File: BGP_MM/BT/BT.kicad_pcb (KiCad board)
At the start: 2 copper layers, 26 x 26 mm, 36 parts, among them J1 Conn_01x02_Male, J2 Conn_01x02_Male, J3 Conn_01x04_Male, J4 Conn_01x04_Male, Q1 MMBF5457, U1 MC33178

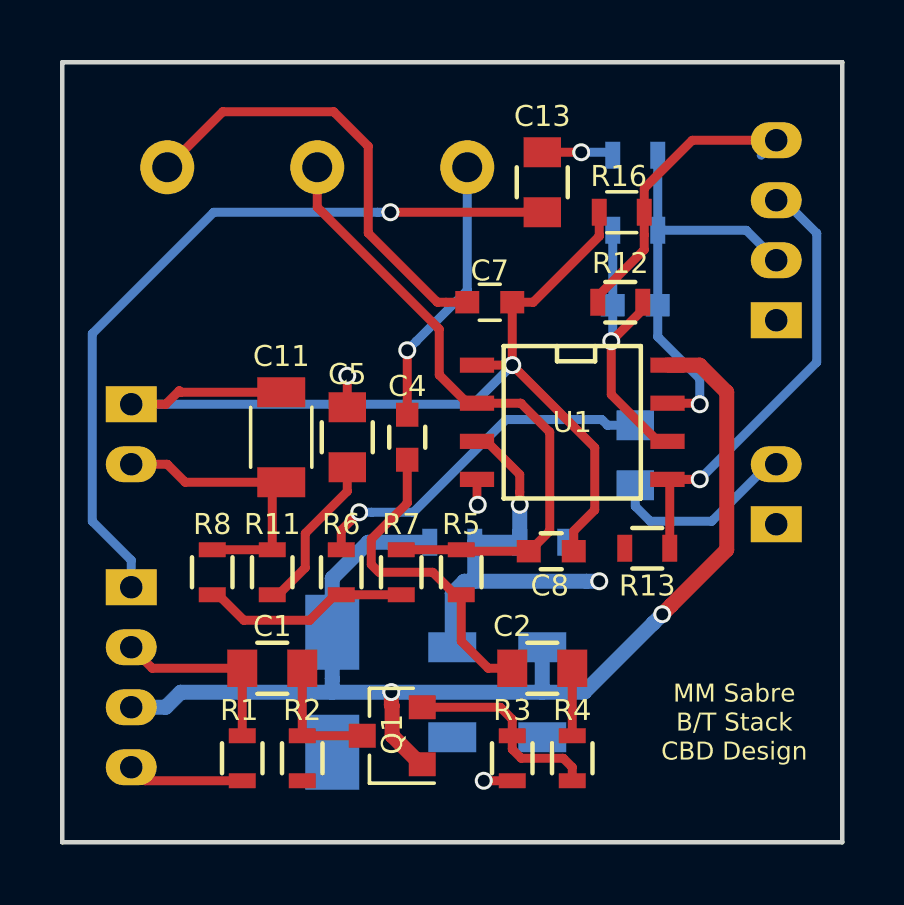
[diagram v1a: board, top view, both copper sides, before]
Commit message: BT Bright Cap/Res changed
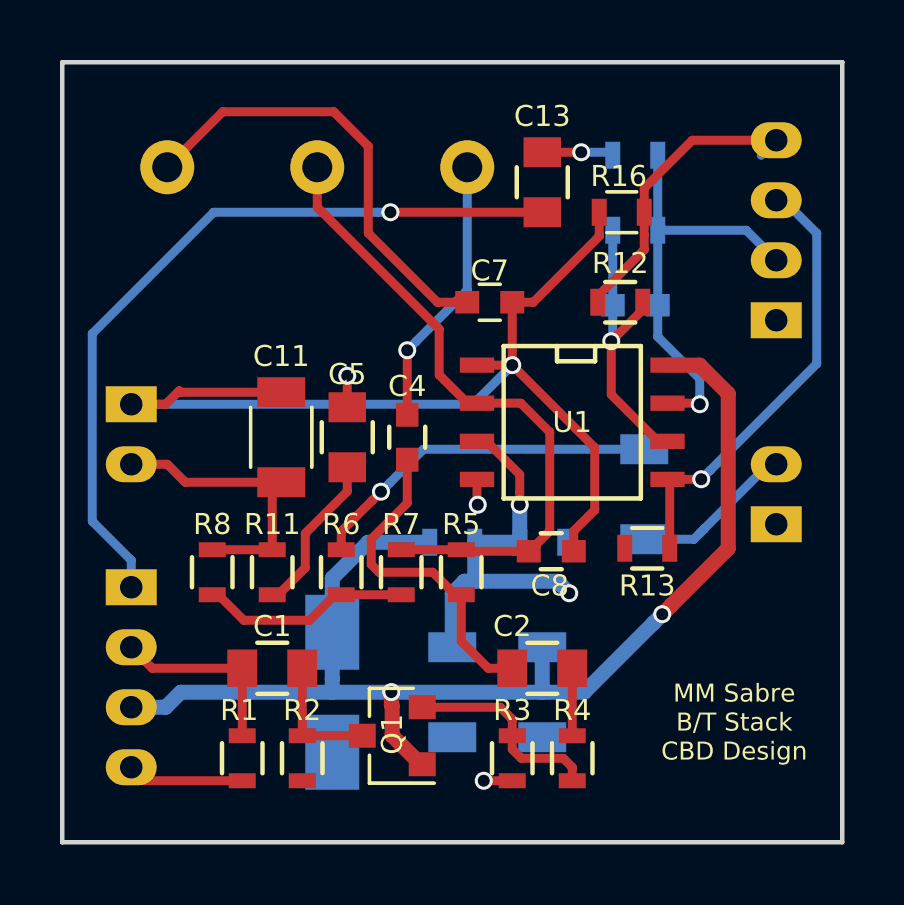
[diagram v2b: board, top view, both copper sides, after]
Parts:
- C3: value 10n -> 22n; footprint Capacitors_SMD:C_0805 -> Capacitors_SMD:C_1206
- R12, R14: value 22k -> 20k
- R6: value 2k -> 1k
- moved C3 1.33 mm to (164.4, 100.4)
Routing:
- net /Vref: track 13.8 -> 13.0 mm
- net Net-(C3-Pad2): track 6.39 -> 5.65 mm

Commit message: MM Refactoring
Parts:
- removed C12: 120p, Capacitors_SMD:C_0603
- removed C13: 1u, Capacitors_SMD:C_0805
- removed J4: Conn_01x04_Male, Connectors_JST:JST_PH_B4B-PH-K_04x2.00mm_Straight
- removed Q1: MMBF5457, TO_SOT_Packages_SMD:SOT-23
- removed R11: 10k, Resistors_SMD:R_0603
- removed R12, R14: 20k, Resistors_SMD:R_0603
- removed R13: 200k, Resistors_SMD:R_0603
- removed R15: 1k, Resistors_SMD:R_0603
- removed R16: 100, Resistors_SMD:R_0603
- added C10: 47n, Capacitors_SMD:C_1206, F.Cu at (165.0, 94.0)
- C1: value 0.1u -> 1u
- C11: value 47n -> 10u; footprint Capacitors_SMD:C_1206 -> Capacitors_SMD:C_0805
- C2: value 1u -> 120p; footprint Capacitors_SMD:C_0805 -> Capacitors_SMD:C_0603_HandSoldering
- C3: moved to F.Cu
- C4: footprint Capacitors_SMD:C_0603 -> Capacitors_SMD:C_0805
- C6, C9: value 47u -> 10u; footprint Capacitors_SMD:C_1206 -> Capacitors_SMD:C_0805
- C7, C8: footprint Capacitors_SMD:C_0603 -> Capacitors_SMD:C_0603_HandSoldering
- J2: value Conn_01x02_Male -> Conn_01x04_Male; footprint Connectors_JST:JST_PH_B2B-PH-K_02x2.00mm_Straight -> Connectors_JST:JST_PH_B4B-PH-K_04x2.00mm_Straight
- J3: value Conn_01x04_Male -> Conn_01x02_Male; footprint Connectors_JST:JST_PH_B4B-PH-K_04x2.00mm_Straight -> Connectors_JST:JST_PH_B2B-PH-K_02x2.00mm_Straight
- R1: footprint Resistors_SMD:R_0603 -> Capacitors_SMD:C_0603_HandSoldering
- R10: value 20k -> 1k; footprint Resistors_SMD:R_0603 -> Capacitors_SMD:C_0603_HandSoldering; moved to F.Cu
- R2: value 1MEG -> 470k; footprint Resistors_SMD:R_0603 -> Capacitors_SMD:C_0603_HandSoldering
- R3: value 20k -> 220k; footprint Resistors_SMD:R_0603 -> Capacitors_SMD:C_0603_HandSoldering
- R4: value 100 -> 1k; footprint Resistors_SMD:R_0603 -> Capacitors_SMD:C_0603_HandSoldering
- R5: value 220k -> 100k; footprint Resistors_SMD:R_0603 -> Capacitors_SMD:C_0603_HandSoldering
- R6: value 1k -> 2k; footprint Resistors_SMD:R_0603 -> Capacitors_SMD:C_0603_HandSoldering
- R7: footprint Resistors_SMD:R_0603 -> Capacitors_SMD:C_0603_HandSoldering; moved to B.Cu
- R8: value 2k -> 100k; footprint Resistors_SMD:R_0603 -> Capacitors_SMD:C_0603_HandSoldering; moved to B.Cu
- R9: value 20k -> 10k; footprint Resistors_SMD:R_0603 -> Capacitors_SMD:C_0603_HandSoldering; moved to F.Cu
- moved R3 13.8 mm to (152.0, 98.0), turned to 90 degrees
- moved C5 12.7 mm to (166.0, 104.0), turned to 270 degrees
- moved R8 11.5 mm to (159.8, 109.0), turned to 180 degrees
- moved J1 11.2 mm to (165.7, 90.6)
- moved C7 11.0 mm to (163.9, 104.0), turned to 90 degrees
- moved R6 10.9 mm to (164.0, 98.0), turned to 270 degrees
- moved C3 9.15 mm to (161.0, 108.9), turned to 90 degrees
- moved R9 9.03 mm to (166.1, 98.0), turned to 270 degrees
- moved U1 8.90 mm to (155.0, 103.5)
- moved C6 8.83 mm to (152.3, 105.5), turned to 0 degrees
- moved C9 7.16 mm to (165.0, 105.5), turned to 0 degrees
- moved R5 5.68 mm to (161.0, 98.0)
- moved R10 5.00 mm to (158.0, 98.0), turned to 90 degrees
- moved J3 4.40 mm to (147.2, 107.9)
- moved R7 4.30 mm to (159.8, 105.5), turned to 0 degrees
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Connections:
- C3 pad 2: Net-(C3-Pad2) -> /BR_O
- C4 pad 1: Net-(C2-Pad2) -> Net-(C2-Pad1)
- C7 pad 2: Net-(C11-Pad2) -> Net-(C10-Pad2)
- C8 pad 2: Net-(C11-Pad2) -> Net-(C10-Pad2)
- J1 pad 1: Earth -> Net-(C10-Pad2)
- J1 pad 2: Net-(C3-Pad2) -> Net-(C10-Pad1)
- J2 pad 1: Net-(C11-Pad2) -> /BR_O
- J2 pad 2: Net-(C11-Pad1) -> /SIG_I
- J3 pad 1: Net-(C13-Pad2) -> Earth
- J3 pad 2: /SIG_I -> VCC
- R1 pad 1: /SIG_I -> Net-(C2-Pad2)
- R1 pad 2: Earth -> Net-(C1-Pad1)
- R10 pad 1: /Vref -> Net-(C11-Pad1)
- R10 pad 2: Earth -> Net-(C10-Pad2)
- R2 pad 1: Net-(C1-Pad1) -> Net-(C2-Pad1)
- R2 pad 2: /Vref -> Net-(C2-Pad2)
- R3 pad 1: Net-(Q1-Pad2) -> Net-(C8-Pad1)
- R3 pad 2: Earth -> Net-(C2-Pad1)
- R4 pad 1: Net-(C2-Pad1) -> Net-(R4-Pad1)
- R4 pad 2: Net-(Q1-Pad2) -> Net-(C3-Pad1)
- R5 pad 1: Net-(C8-Pad1) -> Net-(R4-Pad1)
- R5 pad 2: Net-(C2-Pad2) -> Net-(C8-Pad1)
- R6 pad 1: Net-(R6-Pad1) -> Net-(C10-Pad1)
- R6 pad 2: Net-(C3-Pad1) -> Net-(R4-Pad1)
- R7 pad 1: Net-(R6-Pad1) -> VCC
- R7 pad 2: Net-(C8-Pad1) -> /Vref
- R8 pad 1: Net-(C11-Pad1) -> /Vref
- R8 pad 2: Net-(R6-Pad1) -> Earth
- R9 pad 1: VCC -> Net-(C10-Pad1)
- R9 pad 2: /Vref -> Net-(C5-Pad1)
- U1 pad 1: Net-(C11-Pad2) -> Net-(C2-Pad1)
- U1 pad 2: Net-(C8-Pad1) -> Net-(C2-Pad2)
- U1 pad 5: /Mr -> /Vref
- U1 pad 6: Net-(C12-Pad2) -> Net-(C8-Pad1)
- U1 pad 7: /Mo -> Net-(C10-Pad2)
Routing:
- net /BR_O: track 0.00 -> 32.6 mm, vias 0 -> 1
- net Net-(C10-Pad2): track 0.00 -> 26.7 mm
- net Net-(C13-Pad2): track 25.7 -> 0.00 mm, vias 1 -> 0
- net Net-(C11-Pad2): track 34.5 -> 13.6 mm, vias 1 -> 0
- net Net-(C7-Pad1): track 15.1 -> 31.6 mm, vias 0 -> 1
- net VCC: track 41.6 -> 25.7 mm, vias 2 -> 1
- net Net-(C2-Pad1): track 2.25 -> 17.4 mm
- net /Mr: track 15.1 -> 0.00 mm, vias 1 -> 0
- net /Mo: track 14.3 -> 0.00 mm, vias 1 -> 0
- net Net-(R4-Pad1): track 0.00 -> 14.1 mm
- net /SIG_I: track 6.24 -> 19.3 mm
- net Net-(C10-Pad1): track 0.00 -> 11.7 mm
- net /Mi: track 10.5 -> 0.00 mm
- net Net-(C12-Pad2): track 9.75 -> 0.00 mm, vias 1 -> 0
- net Net-(C8-Pad1): track 21.6 -> 31.3 mm, vias 0 -> 3
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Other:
- board size 26 x 26 mm -> 23 x 26 mm
- board text removed: "MM Sabre B/T Stack CBD Design"

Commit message: MM Refactoring
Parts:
- removed J3: Conn_01x02_Male, Connectors_JST:JST_PH_B2B-PH-K_02x2.00mm_Straight
- C1: value 1u -> 0.1u
- C2: value 120p -> 10p
- C3: value 22n -> 2.7n; footprint Capacitors_SMD:C_1206 -> Capacitors_SMD:C_0805
- C6, C9: footprint Capacitors_SMD:C_0805 -> Capacitors_SMD:C_1206
- J1: footprint Connectors_JST:JST_PH_B2B-PH-K_02x2.00mm_Straight -> Pin_Headers:Pin_Header_Straight_2x01_Pitch2.54mm
- J2: value Conn_01x04_Male -> Conn_01x05_Male; footprint Connectors_JST:JST_PH_B4B-PH-K_04x2.00mm_Straight -> Pin_Headers:Pin_Header_Straight_1x05_Pitch2.54mm
- R10: value 1k -> 100
- R4: value 1k -> 4.7k
- R6: value 2k -> 10k
- U1: value MC33178 -> TS512A
- moved J2 11.0 mm to (148.0, 108.5), turned to 0 degrees
- moved C10 4.34 mm to (161.6, 91.3), turned to 90 degrees
- moved C9 3.50 mm to (165.0, 109.0)
- moved C6 1.02 mm to (153.3, 105.7)
- moved J1 0.92 mm to (165.0, 90.0), turned to 270 degrees
- moved R7 0.51 mm to (159.9, 106.0)
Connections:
- J2 pad 1: /BR_O -> VCC
- J2 pad 2: /SIG_I -> /BR_O
- J2 pad 3: Net-(C11-Pad2) -> /SIG_I
- J2 pad 4: Earth -> Net-(C11-Pad2)
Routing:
- net /BR_O: track 32.6 -> 19.0 mm, vias 1 -> 0
- net /SIG_I: track 19.3 -> 8.33 mm
- net Earth: track 4.61 -> 2.18 mm
- net Net-(C10-Pad1): track 11.7 -> 10.7 mm
- net Net-(C2-Pad1): track 17.4 -> 18.1 mm
- net VCC: track 25.7 -> 25.0 mm
- net Net-(C11-Pad2): track 13.6 -> 13.0 mm
- net Net-(R4-Pad1): track 14.1 -> 13.5 mm

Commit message: MM Gerbers
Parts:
- added R11: 100, Capacitors_SMD:C_0603_HandSoldering, F.Cu at (166.0, 97.0)
- C10: value 47n -> 2.7n; footprint Capacitors_SMD:C_1206 -> Capacitors_SMD:C_0805
- C2: value 10p -> 10u; footprint Capacitors_SMD:C_0603_HandSoldering -> Capacitors_SMD:C_0805
- C4: value 1.8n -> 2.7n
- C5: value 10u -> 10p; footprint Capacitors_SMD:C_0805 -> Capacitors_SMD:C_0603_HandSoldering
- C7: value 470p -> 100p
- C8: value 120p -> 100p
- R2: value 470k -> 10k
- R3: value 220k -> 200k
- R5: value 100k -> 200k
- R9: value 10k -> 200k
- moved R3 17.2 mm to (166.0, 108.0)
- moved C5 16.6 mm to (151.0, 97.0), turned to 90 degrees
- moved C4 12.6 mm to (166.0, 102.0)
- moved C2 12.2 mm to (160.0, 97.0)
- moved R2 12.0 mm to (157.0, 97.0)
- moved R6 11.2 mm to (159.0, 108.0)
- moved R9 11.1 mm to (155.0, 97.0)
- moved C10 10.3 mm to (153.0, 97.0), turned to 270 degrees
- moved C11 10.0 mm to (155.0, 108.0)
- moved R10 10.0 mm to (157.0, 108.0)
- moved R5 5.00 mm to (164.0, 102.0)
- moved C7 4.38 mm to (160.0, 102.0), turned to 270 degrees
- moved C8 2.19 mm to (162.0, 102.0)
- moved C9 1.72 mm to (164.0, 107.6), turned to 90 degrees
- moved C1 1.41 mm to (151.0, 108.0), turned to 90 degrees
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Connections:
- C2 pad 2: Net-(C2-Pad2) -> Earth
- C4 pad 1: Net-(C2-Pad1) -> Net-(C4-Pad1)
- C5 pad 2: Earth -> Net-(C10-Pad1)
- C7 pad 2: Net-(C10-Pad2) -> Net-(C7-Pad2)
- C8 pad 2: Net-(C10-Pad2) -> Net-(C7-Pad2)
- J1 pad 1: Net-(C10-Pad2) -> Net-(C10-Pad1)
- J1 pad 2: Net-(C10-Pad1) -> Net-(C10-Pad2)
- R1 pad 1: Net-(C2-Pad2) -> Net-(C5-Pad1)
- R10 pad 2: Net-(C10-Pad2) -> Net-(C7-Pad2)
- R2 pad 1: Net-(C2-Pad1) -> Net-(C10-Pad2)
- R2 pad 2: Net-(C2-Pad2) -> Net-(C2-Pad1)
- R3 pad 2: Net-(C2-Pad1) -> Net-(C4-Pad1)
- R6 pad 1: Net-(C10-Pad1) -> Net-(C7-Pad2)
- R9 pad 1: Net-(C10-Pad1) -> Net-(C10-Pad2)
- U1 pad 1: Net-(C2-Pad1) -> Net-(C10-Pad1)
- U1 pad 2: Net-(C2-Pad2) -> Net-(C5-Pad1)
- U1 pad 7: Net-(C10-Pad2) -> Net-(C7-Pad2)
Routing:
- net Net-(C10-Pad1): track 10.7 -> 32.8 mm
- net Net-(C2-Pad1): track 18.1 -> 3.89 mm
- net Net-(C2-Pad2): track 13.8 -> 0.00 mm
- net Net-(C7-Pad2): track 0.00 -> 13.1 mm
- net Net-(C7-Pad1): track 31.7 -> 19.0 mm
- net Net-(C5-Pad1): track 4.09 -> 16.5 mm
- net Net-(C10-Pad2): track 27.0 -> 16.3 mm
- net Net-(C4-Pad1): track 0.00 -> 10.5 mm
- net /Vref: track 13.6 -> 17.2 mm, vias 2 -> 3
- net /SIG_I: track 8.33 -> 4.82 mm
- net VCC: track 25.0 -> 22.4 mm
- net Net-(C4-Pad2): track 12.5 -> 14.1 mm, vias 0 -> 1
- net Net-(R4-Pad1): track 13.5 -> 15.2 mm
- net Earth: track 2.18 -> 3.45 mm
- net Net-(C3-Pad1): track 3.35 -> 2.09 mm
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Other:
- net class Default: clearance 0.29 -> 0.25
- rule trace_clearance: 0.29 -> 0.25

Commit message: Minor BOM changes
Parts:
- R9: value 200k -> 180k
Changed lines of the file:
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@@
     (links 45)
     (no_connects 0)
-    (area 143.1 85.37 168.985 112.285)
+    (area 144.924999 85.924999 168.075001 112.075001)
     (thickness 1.6)
     (drawings 8)
@@
       (effects (font (size 0.7 0.7) (thickness 0.15)))
     )
-    (fp_text value 200k (at 0 1.9 270) (layer F.Fab) hide
-      (effects (font (size 0.7 0.7) (thickness 0.15)))
-    )
+    (fp_text value 180k (at 0 1.9 270) (layer F.Fab) hide
+      (effects (font (size 0.7 0.7) (thickness 0.15)))
+    )
